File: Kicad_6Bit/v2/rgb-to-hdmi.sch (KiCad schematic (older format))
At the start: 27 parts, among them J1 Conn_01x03, P1 CONN_02X20, P2 Conn_02x05_Odd_Even, P3 Conn_01x06, P4 CONN_01X02, SW1 SW_PUSH, SW2 SW_PUSH, SW3 SW_PUSH, SW4 SW_PUSH, U1 XC9572XL-VQFP44

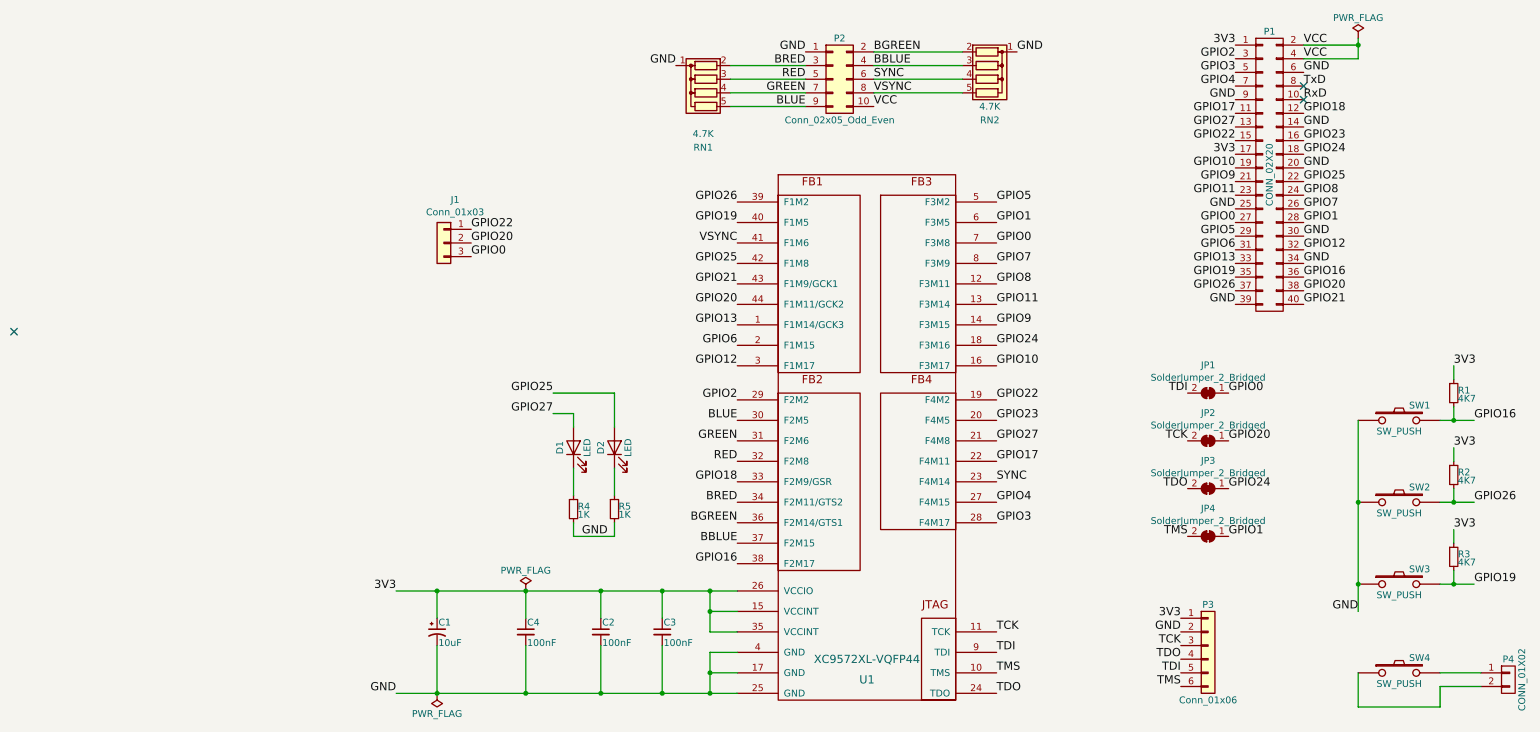
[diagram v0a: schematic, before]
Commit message: Add P19 pin
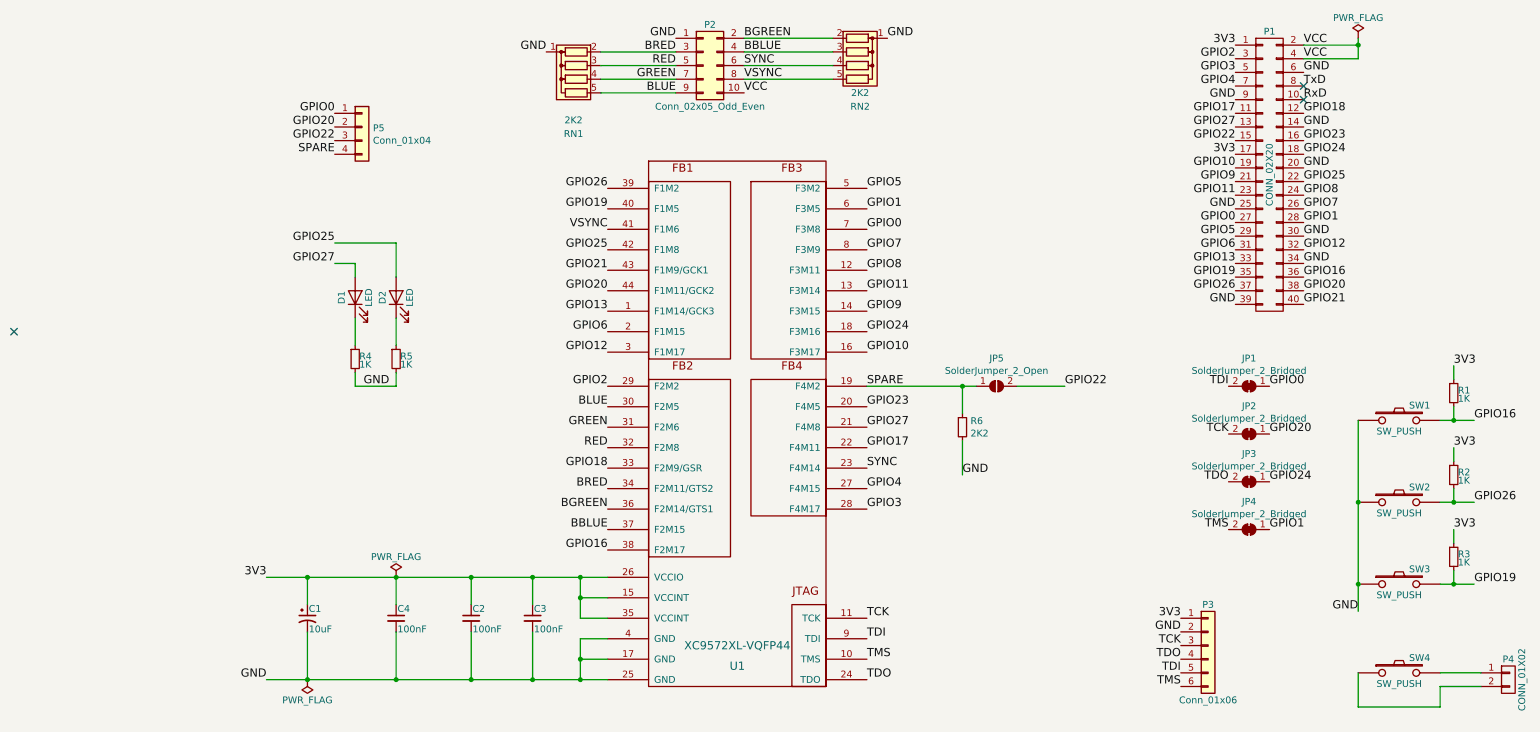
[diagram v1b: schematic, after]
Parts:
- removed J1: Conn_01x03, Connector_PinSocket_2.54mm:PinSocket_1x03_P2.54mm_Vertical, symbol Connector_Generic:Conn_01x03
- added JP5: SolderJumper_2_Open, Jumper:SolderJumper-2_P1.3mm_Open_RoundedPad1.0x1.5mm, symbol Jumper:SolderJumper_2_Open
- added P5: Conn_01x04, Connector_PinSocket_2.54mm:PinSocket_1x04_P2.54mm_Vertical, symbol Connector_Generic:Conn_01x04
- added R6: 2K2, Resistor_SMD:R_0805_2012Metric_Pad1.15x1.40mm_HandSolder, symbol Device:R_Small
- R1, R2, R3: value 4K7 -> 1K
- RN1, RN2: value 4.7K -> 2K2
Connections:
- net GND: now also R6.2
- net GPIO0: now also P5.1 (Pin_1)
- net GPIO20: now also P5.2 (Pin_2)
- net GPIO22: now also JP5.2 (B), P5.3 (Pin_3); no longer U1.19 (F4M2)
- new net SPARE: JP5.1 (A), P5.4 (Pin_4), R6.1, U1.19 (F4M2)
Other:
- moved on the sheet: C1, C2, C3, C4, D1, D2, JP1, JP2, JP3, JP4, P2, R4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

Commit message: Change CLK to CLKEN
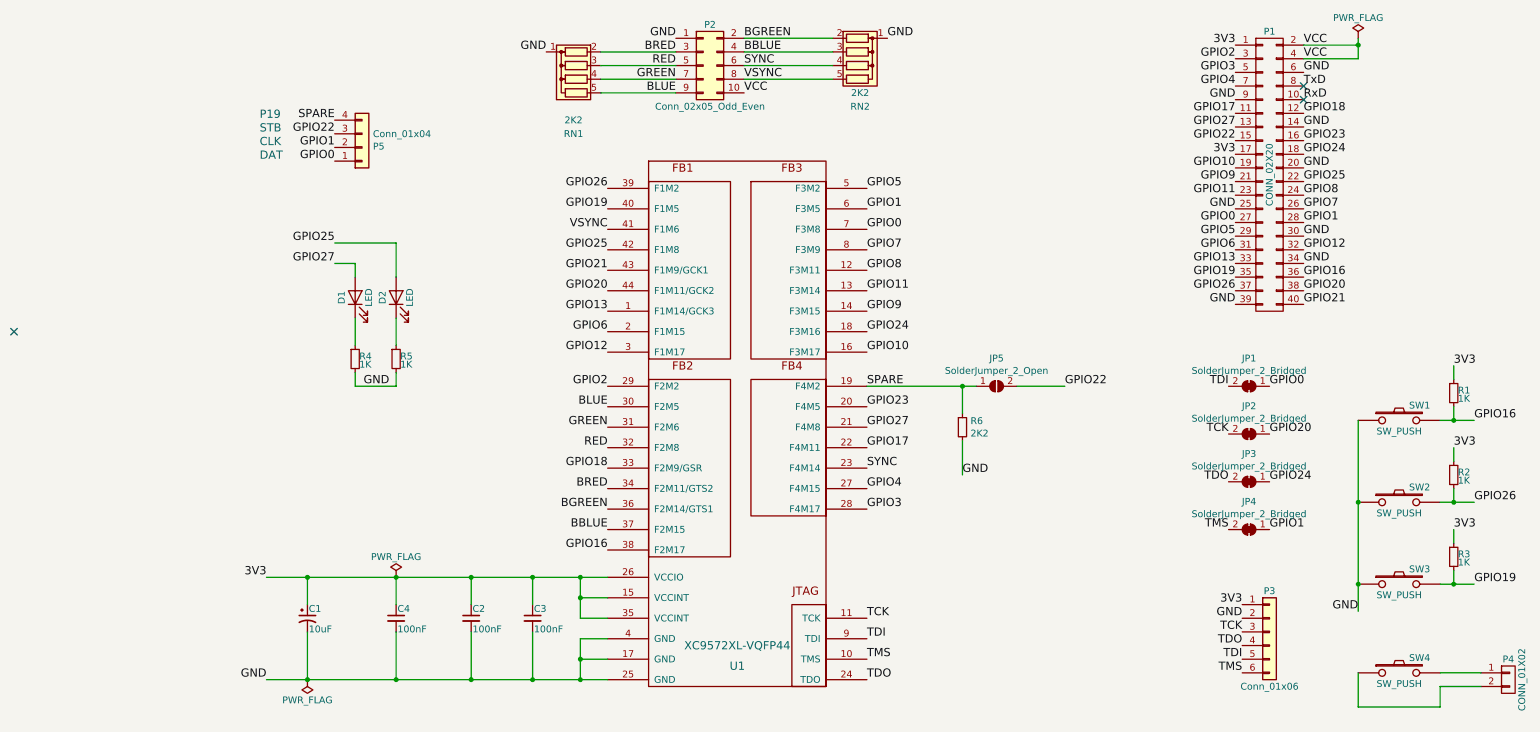
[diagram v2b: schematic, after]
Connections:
- net GPIO1: now also P5.2 (Pin_2)
- net GPIO20: no longer P5.2 (Pin_2)
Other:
- note added: "CLK"
- note added: "DAT"
- note added: "P19\n"
- note added: "STB"
- moved on the sheet: P3, P5
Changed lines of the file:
@@
 L rgb-to-hdmi-rescue:Conn_01x06 P3
 U 1 1 5DA9B6A9
-P 8250 5550
-F 0 "P3" H 8250 5850 50  0000 C CNN
-F 1 "Conn_01x06" H 8250 5150 50  0000 C CNN
-F 2 "Connector_PinHeader_2.54mm:PinHeader_1x06_P2.54mm_Vertical" H 8250 5550 50  0001 C CNN
-F 3 "" H 8250 5550 50  0001 C CNN
-	1    8250 5550
-	1    0    0    -1
-$EndComp
-Text Label 8050 5350 2    60   ~ 0
+P 8700 5450
+F 0 "P3" H 8700 5750 50  0000 C CNN
+F 1 "Conn_01x06" H 8700 5050 50  0000 C CNN
+F 2 "Connector_PinHeader_2.54mm:PinHeader_1x06_P2.54mm_Vertical" H 8700 5450 50  0001 C CNN
+F 3 "" H 8700 5450 50  0001 C CNN
+	1    8700 5450
+	1    0    0    -1
+$EndComp
+Text Label 8500 5250 2    60   ~ 0
 3V3
-Text Label 8050 5450 2    60   ~ 0
+Text Label 8500 5350 2    60   ~ 0
 GND
-Text Label 8050 5550 2    60   ~ 0
+Text Label 8500 5450 2    60   ~ 0
 TCK
-Text Label 8050 5650 2    60   ~ 0
+Text Label 8500 5550 2    60   ~ 0
 TDO
-Text Label 8050 5750 2    60   ~ 0
+Text Label 8500 5650 2    60   ~ 0
 TDI
-Text Label 8050 5850 2    60   ~ 0
+Text Label 8500 5750 2    60   ~ 0
 TMS
 Text Label 5750 5350 0    60   ~ 0
@@
 L Connector_Generic:Conn_01x04 P5
 U 1 1 5DCE6A21
-P 2050 1750
-F 0 "P5" H 2130 1742 50  0000 L CNN
-F 1 "Conn_01x04" H 2130 1651 50  0000 L CNN
-F 2 "Connector_PinSocket_2.54mm:PinSocket_1x04_P2.54mm_Vertical" H 2050 1750 50  0001 C CNN
-F 3 "~" H 2050 1750 50  0001 C CNN
-	1    2050 1750
-	1    0    0    -1
-$EndComp
-Text Label 1850 1650 2    60   ~ 0
+P 2050 1900
+F 0 "P5" H 2130 1892 50  0000 L CNN
+F 1 "Conn_01x04" H 2130 1801 50  0000 L CNN
+F 2 "Connector_PinSocket_2.54mm:PinSocket_1x04_P2.54mm_Vertical" H 2050 1900 50  0001 C CNN
+F 3 "~" H 2050 1900 50  0001 C CNN
+	1    2050 1900
+	1    0    0    1
+$EndComp
+Text Label 1850 2000 2    60   ~ 0
 GPIO0
-Text Label 1850 1750 2    60   ~ 0
-GPIO20
-Text Label 1850 1850 2    60   ~ 0
+Text Label 1850 1900 2    60   ~ 0
+GPIO1
+Text Label 1850 1800 2    60   ~ 0
 GPIO22
-Text Label 1850 1950 2    60   ~ 0
+Text Label 1850 1700 2    60   ~ 0
 SPARE
 Wire Wire Line
@@
 	1    0    0    -1
 $EndComp
+Text Notes 1300 2000 0    60   ~ 0
+DAT
+Text Notes 1300 1900 0    60   ~ 0
+CLK
+Text Notes 1300 1800 0    60   ~ 0
+STB
+Text Notes 1300 1700 0    60   ~ 0
+P19\n
 $EndSCHEMATC

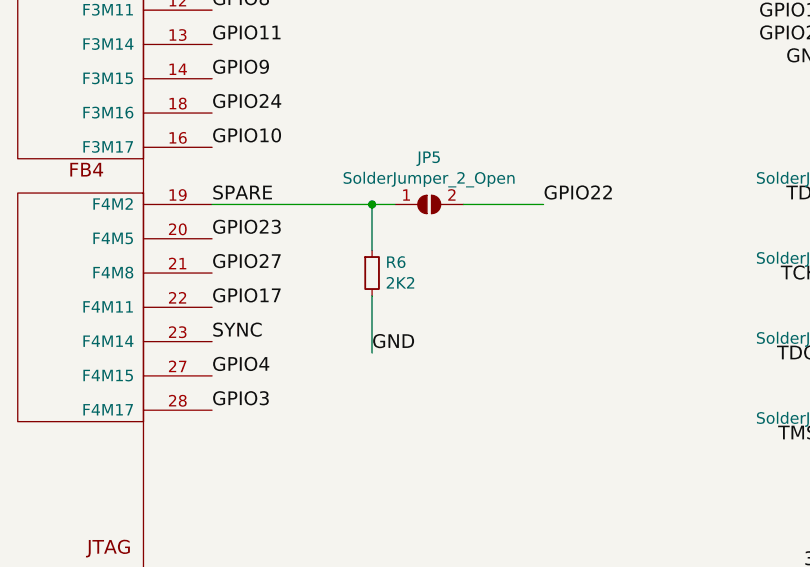
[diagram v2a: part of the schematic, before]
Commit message: Change value of R5 from 2K2 to 10K
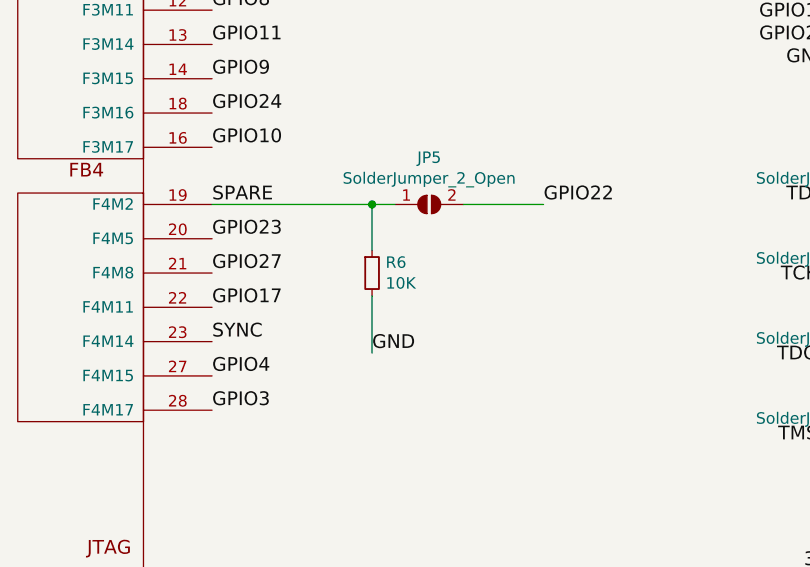
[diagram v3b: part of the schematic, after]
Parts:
- R6: value 2K2 -> 10K
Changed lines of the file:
@@
 P 6450 3950
 F 0 "R6" H 6509 3996 50  0000 L CNN
-F 1 "2K2" H 6509 3905 50  0000 L CNN
+F 1 "10K" H 6509 3905 50  0000 L CNN
 F 2 "Resistor_SMD:R_0805_2012Metric_Pad1.15x1.40mm_HandSolder" H 6450 3950 50  0001 C CNN
 F 3 "~" H 6450 3950 50  0001 C CNN

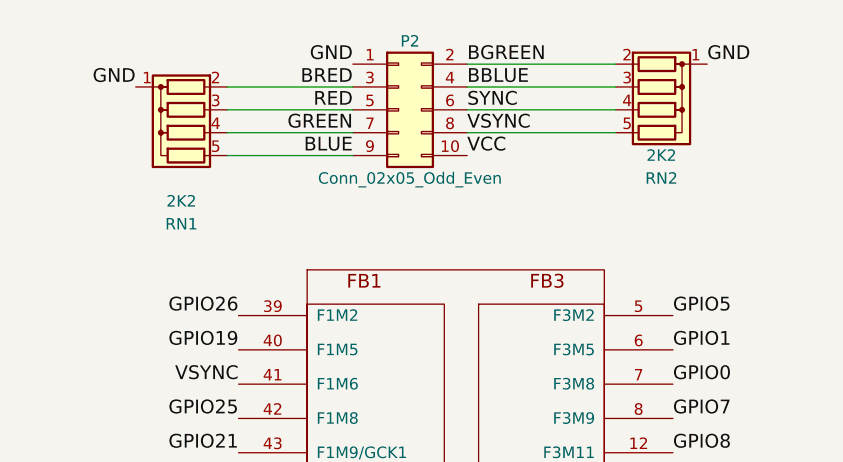
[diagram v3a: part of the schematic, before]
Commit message: Change RN1&2 to 4K7
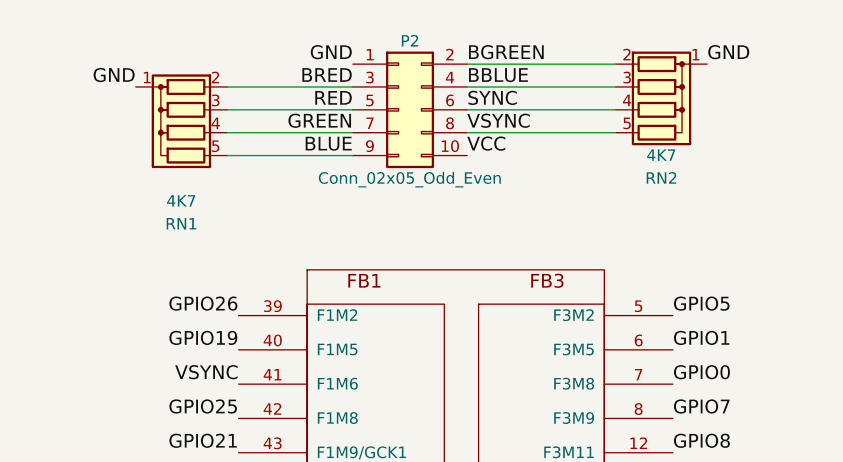
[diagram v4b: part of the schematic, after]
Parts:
- RN1, RN2: value 2K2 -> 4K7
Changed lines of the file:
@@
 P 3600 1400
 F 0 "RN1" V 4000 1400 50  0000 C CNN
-F 1 "2K2" V 3900 1400 50  0000 C CNN
+F 1 "4K7" V 3900 1400 50  0000 C CNN
 F 2 "Resistor_THT:R_Array_SIP5" V 3875 1400 50  0001 C CNN
 F 3 "" H 3600 1400 50  0001 C CNN
@@
 P 5700 1300
 F 0 "RN2" V 6000 1300 50  0000 C CNN
-F 1 "2K2" V 5900 1300 50  0000 C CNN
+F 1 "4K7" V 5900 1300 50  0000 C CNN
 F 2 "Resistor_THT:R_Array_SIP5" V 5975 1300 50  0001 C CNN
 F 3 "" H 5700 1300 50  0001 C CNN
